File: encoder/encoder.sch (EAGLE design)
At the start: 6 parts, among them U1 AH_3761, U2 AH_3761

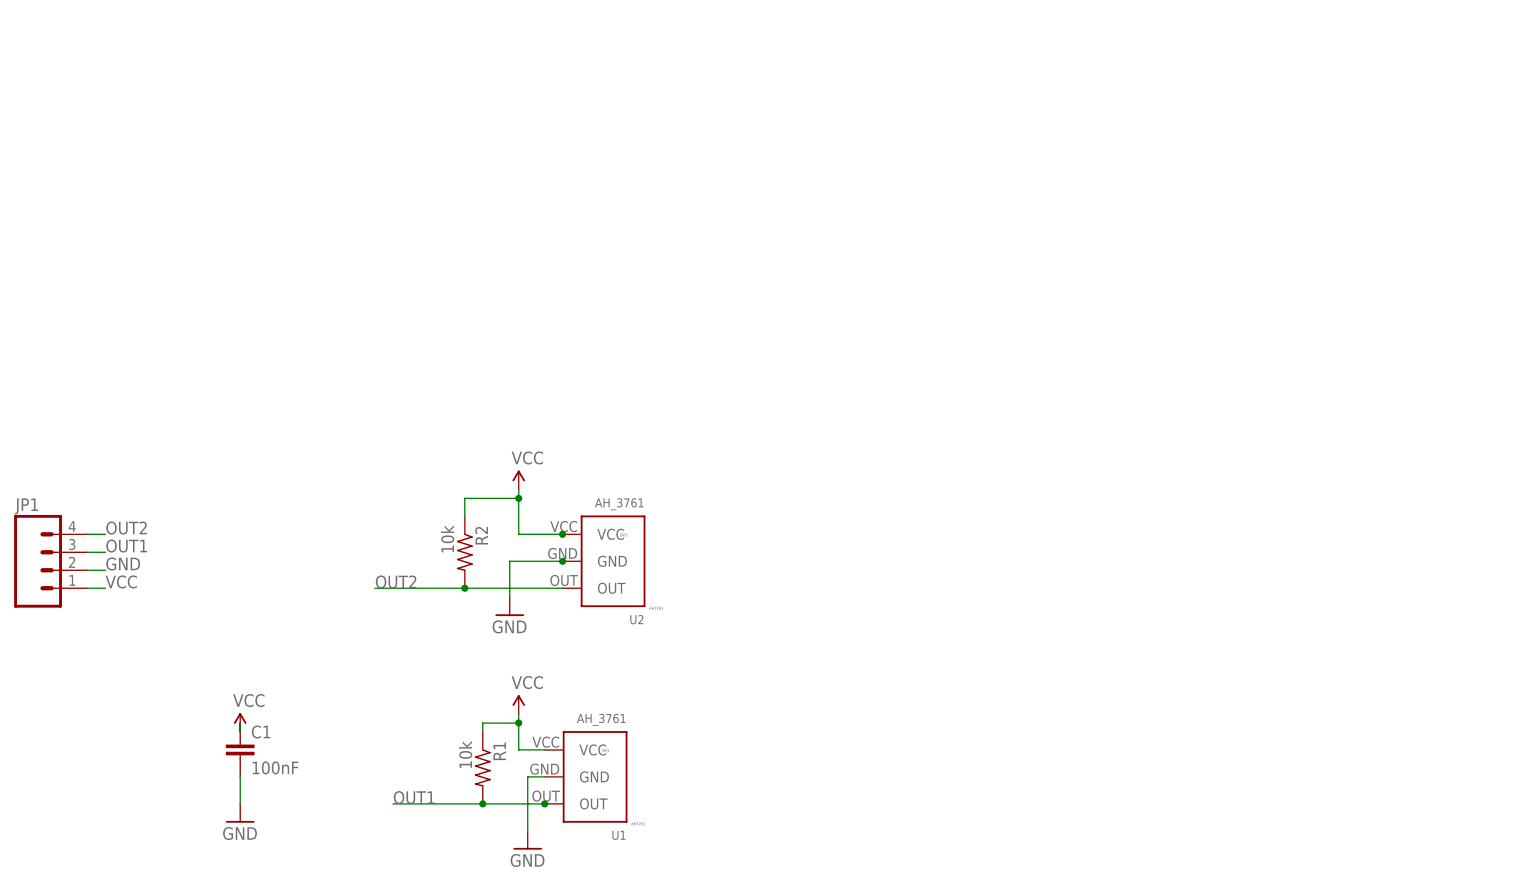
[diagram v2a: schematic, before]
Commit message: Fix all schematics to have a frame and be in quadrant I
Change-Id: I9709ffe2e940512e8f74172f888a837b658cad74
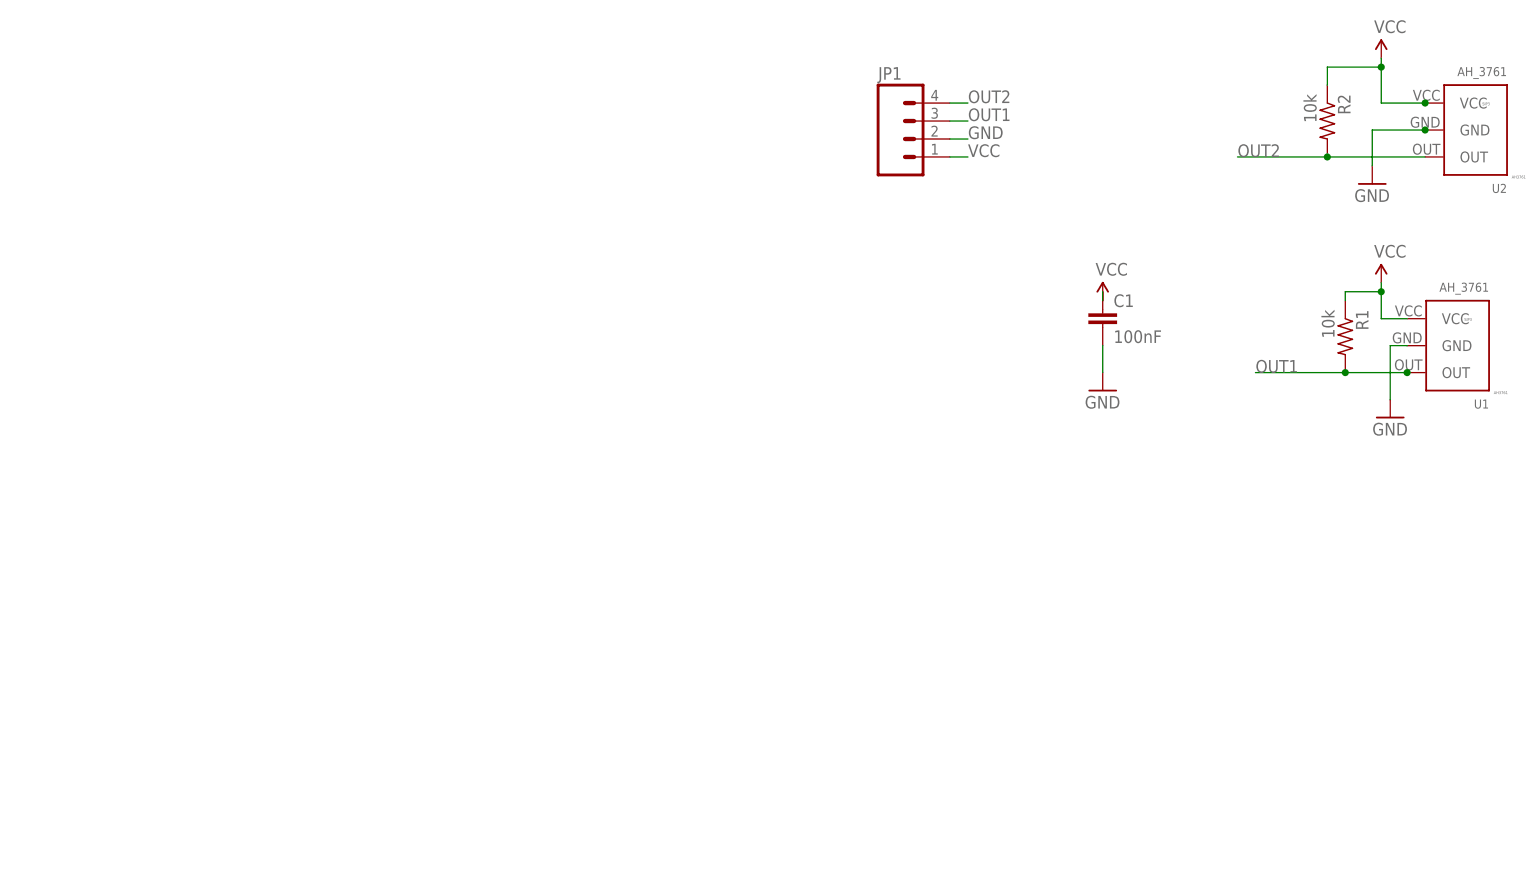
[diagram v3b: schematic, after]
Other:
- moved on the sheet: C1, JP1, R1, R2, U1, U2
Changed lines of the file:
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@@
 <part name="P+2" library="SparkFun-Aesthetics" deviceset="VCC" device=""/>
 <part name="JP1" library="pie" deviceset="M04" device="POLAR"/>
+<part name="FRAME1" library="pie" deviceset="FRAME-LETTER" device="">
+<attribute name="AUTHOR" value="Chris Buonocore"/>
+<attribute name="REVISION" value="B"/>
+</part>
 </parts>
 <sheets>
@@
 </plain>
 <instances>
-<instance part="U2" gate="G$1" x="12.7" y="26.67" rot="R180"/>
-<instance part="R1" gate="G$1" x="-2.54" y="-2.54" rot="R270"/>
-<instance part="C1" gate="G$1" x="-36.83" y="-1.27"/>
-<instance part="R2" gate="G$1" x="-5.08" y="27.94" rot="R270"/>
-<instance part="U1" gate="G$1" x="10.16" y="-3.81" rot="R180"/>
-<instance part="GND1" gate="1" x="3.81" y="-13.97"/>
-<instance part="GND2" gate="1" x="1.27" y="19.05"/>
-<instance part="GND3" gate="1" x="-36.83" y="-10.16"/>
-<instance part="P+1" gate="1" x="-36.83" y="2.54"/>
-<instance part="P+3" gate="1" x="2.54" y="5.08"/>
-<instance part="P+2" gate="1" x="2.54" y="36.83"/>
-<instance part="JP1" gate="G$1" x="-63.5" y="25.4"/>
+<instance part="U2" gate="G$1" x="134.62" y="87.63" rot="R180"/>
+<instance part="R1" gate="G$1" x="119.38" y="58.42" rot="R270"/>
+<instance part="C1" gate="G$1" x="85.09" y="59.69"/>
+<instance part="R2" gate="G$1" x="116.84" y="88.9" rot="R270"/>
+<instance part="U1" gate="G$1" x="132.08" y="57.15" rot="R180"/>
+<instance part="GND1" gate="1" x="125.73" y="46.99"/>
+<instance part="GND2" gate="1" x="123.19" y="80.01"/>
+<instance part="GND3" gate="1" x="85.09" y="50.8"/>
+<instance part="P+1" gate="1" x="85.09" y="63.5"/>
+<instance part="P+3" gate="1" x="124.46" y="66.04"/>
+<instance part="P+2" gate="1" x="124.46" y="97.79"/>
+<instance part="JP1" gate="G$1" x="58.42" y="86.36"/>
+<instance part="FRAME1" gate="G$1" x="0" y="0"/>
+<instance part="FRAME1" gate="G$2" x="147.32" y="0">
+<attribute name="AUTHOR" x="147.32" y="0" size="1.778" layer="96" display="off"/>
+<attribute name="REVISION" x="147.32" y="0" size="1.778" layer="96" display="off"/>
+</instance>
 </instances>
 <busses>
@@
 <segment>
 <pinref part="U2" gate="G$1" pin="OUT"/>
-<wire x1="-17.78" y1="22.86" x2="-5.08" y2="22.86" width="0.1524" layer="91"/>
-<label x="-17.78" y="22.86" size="1.778" layer="95"/>
+<wire x1="104.14" y1="83.82" x2="116.84" y2="83.82" width="0.1524" layer="91"/>
+<label x="104.14" y="83.82" size="1.778" layer="95"/>
 <pinref part="R2" gate="G$1" pin="2"/>
-<wire x1="-5.08" y1="22.86" x2="8.74" y2="22.86" width="0.1524" layer="91"/>
-<junction x="-5.08" y="22.86"/>
+<wire x1="116.84" y1="83.82" x2="130.66" y2="83.82" width="0.1524" layer="91"/>
+<junction x="116.84" y="83.82"/>
 </segment>
 <segment>
 <pinref part="JP1" gate="G$1" pin="4"/>
-<wire x1="-58.42" y1="30.48" x2="-55.88" y2="30.48" width="0.1524" layer="91"/>
-<label x="-55.88" y="30.48" size="1.778" layer="95"/>
+<wire x1="63.5" y1="91.44" x2="66.04" y2="91.44" width="0.1524" layer="91"/>
+<label x="66.04" y="91.44" size="1.778" layer="95"/>
 </segment>
 </net>
 <net name="OUT1" class="0">
 <segment>
-<wire x1="6.35" y1="-7.62" x2="6.2" y2="-7.62" width="0.1524" layer="91"/>
-<label x="-15.24" y="-7.62" size="1.778" layer="95"/>
+<wire x1="128.27" y1="53.34" x2="128.12" y2="53.34" width="0.1524" layer="91"/>
+<label x="106.68" y="53.34" size="1.778" layer="95"/>
 <pinref part="R1" gate="G$1" pin="2"/>
-<wire x1="6.2" y1="-7.62" x2="-2.54" y2="-7.62" width="0.1524" layer="91"/>
-<wire x1="-2.54" y1="-7.62" x2="-15.24" y2="-7.62" width="0.1524" layer="91"/>
-<junction x="-2.54" y="-7.62"/>
+<wire x1="128.12" y1="53.34" x2="119.38" y2="53.34" width="0.1524" layer="91"/>
+<wire x1="119.38" y1="53.34" x2="106.68" y2="53.34" width="0.1524" layer="91"/>
+<junction x="119.38" y="53.34"/>
 <pinref part="U1" gate="G$1" pin="OUT"/>
-<junction x="6.2" y="-7.62"/>
+<junction x="128.12" y="53.34"/>
 </segment>
 <segment>
 <pinref part="JP1" gate="G$1" pin="3"/>
-<wire x1="-55.88" y1="27.94" x2="-58.42" y2="27.94" width="0.1524" layer="91"/>
-<label x="-55.88" y="27.94" size="1.778" layer="95"/>
+<wire x1="66.04" y1="88.9" x2="63.5" y2="88.9" width="0.1524" layer="91"/>
+<label x="66.04" y="88.9" size="1.778" layer="95"/>
 </segment>
 </net>
@@
 <segment>
 <pinref part="U1" gate="G$1" pin="VCC"/>
-<wire x1="6.2" y1="0" x2="2.54" y2="0" width="0.1524" layer="91"/>
+<wire x1="128.12" y1="60.96" x2="124.46" y2="60.96" width="0.1524" layer="91"/>
 <pinref part="P+3" gate="1" pin="VCC"/>
-<wire x1="2.54" y1="0" x2="2.54" y2="3.81" width="0.1524" layer="91"/>
+<wire x1="124.46" y1="60.96" x2="124.46" y2="64.77" width="0.1524" layer="91"/>
 <pinref part="R1" gate="G$1" pin="1"/>
-<wire x1="2.54" y1="3.81" x2="2.54" y2="5.08" width="0.1524" layer="91"/>
-<wire x1="-2.54" y1="2.54" x2="-2.54" y2="3.81" width="0.1524" layer="91"/>
-<wire x1="-2.54" y1="3.81" x2="2.54" y2="3.81" width="0.1524" layer="91"/>
-<junction x="2.54" y="3.81"/>
+<wire x1="124.46" y1="64.77" x2="124.46" y2="66.04" width="0.1524" layer="91"/>
+<wire x1="119.38" y1="63.5" x2="119.38" y2="64.77" width="0.1524" layer="91"/>
+<wire x1="119.38" y1="64.77" x2="124.46" y2="64.77" width="0.1524" layer="91"/>
+<junction x="124.46" y="64.77"/>
 </segment>
 <segment>
 <pinref part="P+2" gate="1" pin="VCC"/>
-<wire x1="2.54" y1="30.48" x2="2.54" y2="35.56" width="0.1524" layer="91"/>
+<wire x1="124.46" y1="91.44" x2="124.46" y2="96.52" width="0.1524" layer="91"/>
 <pinref part="R2" gate="G$1" pin="1"/>
-<wire x1="2.54" y1="35.56" x2="2.54" y2="36.83" width="0.1524" layer="91"/>
-<wire x1="-5.08" y1="33.02" x2="-5.08" y2="35.56" width="0.1524" layer="91"/>
-<wire x1="-5.08" y1="35.56" x2="2.54" y2="35.56" width="0.1524" layer="91"/>
-<junction x="2.54" y="35.56"/>
-<wire x1="2.54" y1="30.48" x2="8.74" y2="30.48" width="0.1524" layer="91"/>
+<wire x1="124.46" y1="96.52" x2="124.46" y2="97.79" width="0.1524" layer="91"/>
+<wire x1="116.84" y1="93.98" x2="116.84" y2="96.52" width="0.1524" layer="91"/>
+<wire x1="116.84" y1="96.52" x2="124.46" y2="96.52" width="0.1524" layer="91"/>
+<junction x="124.46" y="96.52"/>
+<wire x1="124.46" y1="91.44" x2="130.66" y2="91.44" width="0.1524" layer="91"/>
 <pinref part="U2" gate="G$1" pin="VCC"/>
-<wire x1="8.74" y1="30.48" x2="8.89" y2="30.48" width="0.1524" layer="91"/>
-<junction x="8.74" y="30.48"/>
+<wire x1="130.66" y1="91.44" x2="130.81" y2="91.44" width="0.1524" layer="91"/>
+<junction x="130.66" y="91.44"/>
 </segment>
 <segment>
 <pinref part="C1" gate="G$1" pin="1"/>
 <pinref part="P+1" gate="1" pin="VCC"/>
-<wire x1="-36.83" y1="3.81" x2="-36.83" y2="2.54" width="0.1524" layer="91"/>
+<wire x1="85.09" y1="64.77" x2="85.09" y2="63.5" width="0.1524" layer="91"/>
 </segment>
 <segment>
 <pinref part="JP1" gate="G$1" pin="1"/>
-<wire x1="-55.88" y1="22.86" x2="-58.42" y2="22.86" width="0.1524" layer="91"/>
-<label x="-55.88" y="22.86" size="1.778" layer="95"/>
+<wire x1="66.04" y1="83.82" x2="63.5" y2="83.82" width="0.1524" layer="91"/>
+<label x="66.04" y="83.82" size="1.778" layer="95"/>
 </segment>
 </net>
@@
 <segment>
 <pinref part="GND2" gate="1" pin="GND"/>
-<wire x1="1.27" y1="21.59" x2="1.27" y2="26.67" width="0.1524" layer="91"/>
-<wire x1="1.27" y1="26.67" x2="8.74" y2="26.67" width="0.1524" layer="91"/>
+<wire x1="123.19" y1="82.55" x2="123.19" y2="87.63" width="0.1524" layer="91"/>
+<wire x1="123.19" y1="87.63" x2="130.66" y2="87.63" width="0.1524" layer="91"/>
 <pinref part="U2" gate="G$1" pin="GND"/>
-<wire x1="8.74" y1="26.67" x2="8.89" y2="26.67" width="0.1524" layer="91"/>
-<junction x="8.74" y="26.67"/>
+<wire x1="130.66" y1="87.63" x2="130.81" y2="87.63" width="0.1524" layer="91"/>
+<junction x="130.66" y="87.63"/>
 </segment>
 <segment>
-<wire x1="6.2" y1="-3.81" x2="3.81" y2="-3.81" width="0.1524" layer="91"/>
+<wire x1="128.12" y1="57.15" x2="125.73" y2="57.15" width="0.1524" layer="91"/>
 <pinref part="U1" gate="G$1" pin="GND"/>
 <pinref part="GND1" gate="1" pin="GND"/>
-<wire x1="3.81" y1="-11.43" x2="3.81" y2="-3.81" width="0.1524" layer="91"/>
+<wire x1="125.73" y1="49.53" x2="125.73" y2="57.15" width="0.1524" layer="91"/>
 </segment>
 <segment>
 <pinref part="C1" gate="G$1" pin="2"/>
 <pinref part="GND3" gate="1" pin="GND"/>
-<wire x1="-36.83" y1="-3.81" x2="-36.83" y2="-7.62" width="0.1524" layer="91"/>
+<wire x1="85.09" y1="57.15" x2="85.09" y2="53.34" width="0.1524" layer="91"/>
 </segment>
 <segment>
 <pinref part="JP1" gate="G$1" pin="2"/>
-<wire x1="-55.88" y1="25.4" x2="-58.42" y2="25.4" width="0.1524" layer="91"/>
-<label x="-55.88" y="25.4" size="1.778" layer="95"/>
+<wire x1="66.04" y1="86.36" x2="63.5" y2="86.36" width="0.1524" layer="91"/>
+<label x="66.04" y="86.36" size="1.778" layer="95"/>
 </segment>
 </net>
